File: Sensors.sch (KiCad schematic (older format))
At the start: 70 parts, among them CN3 CONN_HEADER_SMD_4POS_2MM, CN4 CONN_HEADER_SMD_4POS_2MM, U1 LPS25HB, U10 MPXV4006GP, U11 MPXV4006DP, U12 TLV2333IDR, U17 MPXV4006GP

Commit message: Annotation has been done
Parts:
- gave numbers to parts that had none: 43

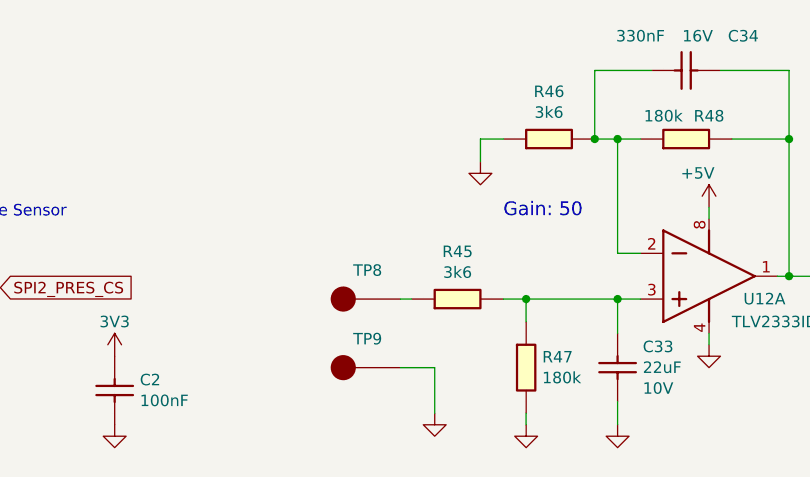
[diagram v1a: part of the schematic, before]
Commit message: added connectors for oxygen sensor and speakers molex 2.54mm pitch vertical
connectors have been added for oxygen sensor and speakers. thery are molex vertical connector 2.54mm pitch vertical. please let me know if any other part is desirable to be used instead.
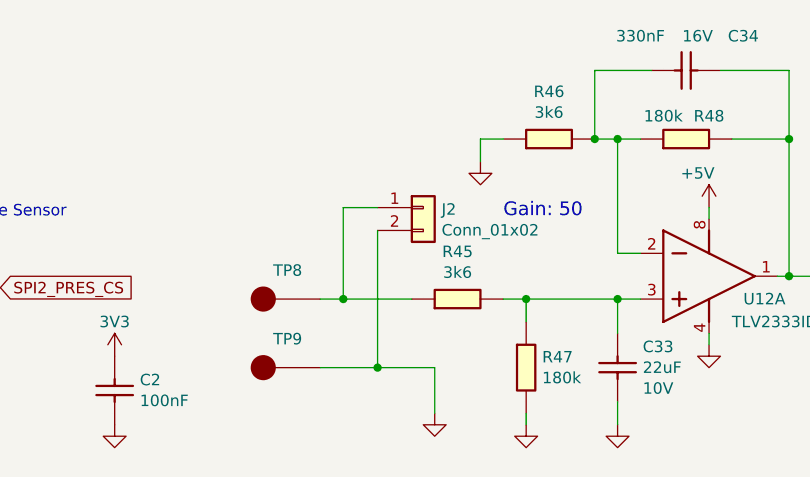
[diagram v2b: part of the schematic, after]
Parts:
- added J2: Conn_01x02, Connector_PinSocket_2.54mm:PinSocket_1x02_P2.54mm_Vertical, symbol Connector_Generic:Conn_01x02
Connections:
- net GND: now also J2.2 (Pin_2)
- net at R45.1, TP8.1: now also J2.1 (Pin_1)
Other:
- moved on the sheet: TP8, TP9
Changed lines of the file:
@@
 	2700 2100 2300 2100
 Wire Wire Line
-	4600 7250 4450 7250
-Wire Wire Line
 	4600 7450 4600 7250
-Wire Wire Line
-	4500 6950 4450 6950
 Wire Wire Line
 	5400 6950 5500 6950
@@
 L OpenVent:Test_Point_PTH TP8
 U 1 1 5FCEC103
-P 4450 6950
-F 0 "TP8" H 4307 7075 50  0000 C CNN
-F 1 "Test_Point_PTH" H 4450 6950 50  0001 C CNN
-F 2 "TestPoint:TestPoint_Pad_2.0x2.0mm" H 4450 6950 50  0001 C CNN
-F 3 "" H 4450 6950 50  0001 C CNN
-	1    4450 6950
+P 4100 6950
+F 0 "TP8" H 3957 7075 50  0000 C CNN
+F 1 "Test_Point_PTH" H 4100 6950 50  0001 C CNN
+F 2 "TestPoint:TestPoint_Pad_2.0x2.0mm" H 4100 6950 50  0001 C CNN
+F 3 "" H 4100 6950 50  0001 C CNN
+	1    4100 6950
 	1    0    0    -1
 $EndComp
@@
 L OpenVent:Test_Point_PTH TP9
 U 1 1 5FCECBB9
-P 4450 7250
-F 0 "TP9" H 4307 7375 50  0000 C CNN
-F 1 "Test_Point_PTH" H 4450 7250 50  0001 C CNN
-F 2 "TestPoint:TestPoint_Pad_2.0x2.0mm" H 4450 7250 50  0001 C CNN
-F 3 "" H 4450 7250 50  0001 C CNN
-	1    4450 7250
+P 4100 7250
+F 0 "TP9" H 3957 7375 50  0000 C CNN
+F 1 "Test_Point_PTH" H 4100 7250 50  0001 C CNN
+F 2 "TestPoint:TestPoint_Pad_2.0x2.0mm" H 4100 7250 50  0001 C CNN
+F 3 "" H 4100 7250 50  0001 C CNN
+	1    4100 7250
 	1    0    0    -1
 $EndComp
@@
 Text Notes 6450 4050 0    75   ~ 15
 FPGA ADC analog circuitry
+Wire Wire Line
+	4100 7250 4350 7250
+Wire Wire Line
+	4350 6650 4350 7250
+Connection ~ 4350 7250
+Wire Wire Line
+	4350 7250 4600 7250
+Wire Wire Line
+	4350 6550 4200 6550
+Wire Wire Line
+	4200 6550 4200 6950
+Wire Wire Line
+	4100 6950 4200 6950
+Connection ~ 4200 6950
+Wire Wire Line
+	4200 6950 4500 6950
+$Comp
+L Connector_Generic:Conn_01x02 J2
+U 1 1 609D2D12
+P 4550 6550
+AR Path="/5F8F3873/609D2D12" Ref="J2"  Part="1"
+AR Path="/60D4F569/609D2D12" Ref="J?"  Part="1"
+F 0 "J2" H 4630 6542 50  0000 L CNN
+F 1 "Conn_01x02" H 4630 6451 50  0000 L CNN
+F 2 "Connector_PinSocket_2.54mm:PinSocket_1x02_P2.54mm_Vertical" H 4550 6550 50  0001 C CNN
+F 3 "http://www.farnell.com/datasheets/2695416.pdf" H 4550 6550 50  0001 C CNN
+	1    4550 6550
+	1    0    0    -1
+$EndComp
 $EndSCHEMATC

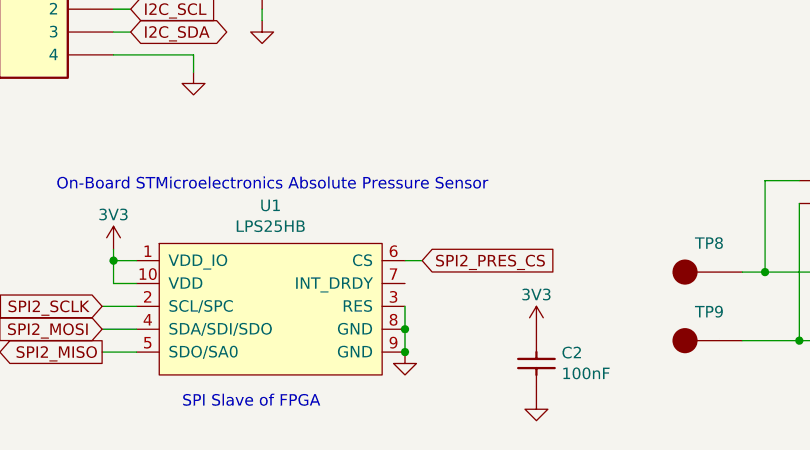
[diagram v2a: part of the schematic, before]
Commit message: Beginning the process of design review, fixed a couple howlers.
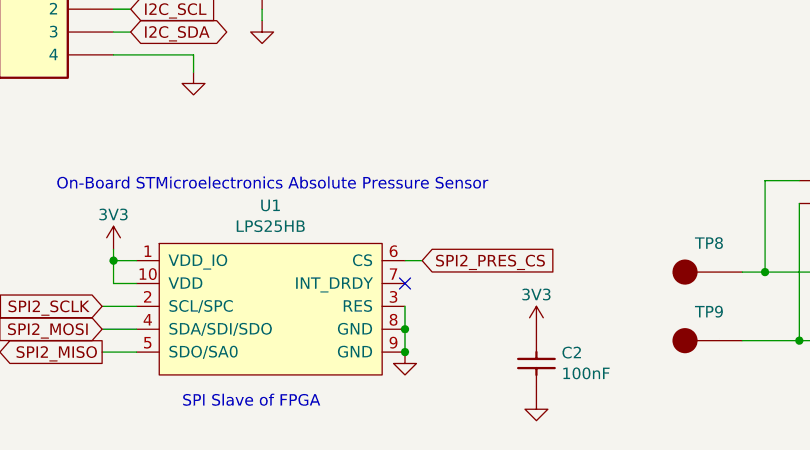
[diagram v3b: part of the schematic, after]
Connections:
- no-connect marks 1 -> 2
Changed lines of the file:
@@
 	1    0    0    -1
 $EndComp
+NoConn ~ 2625 7000
 $EndSCHEMATC

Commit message: add footprint
new footprint was added to parts without footprint
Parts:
- FB4: value Chip_Ferrite,_600R,_0603,_750mA -> BLM18AG601SN1D Chip_Ferrite,_600R,_0603,_750mA; footprint (none) -> Capacitor_SMD:C_0603_1608Metric
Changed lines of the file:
@@
 AR Path="/5F8F3873/61F2C4AF" Ref="FB4"  Part="1"
 F 0 "FB4" H 6900 1800 50  0000 C CNN
-F 1 "Chip_Ferrite,_600R,_0603,_750mA" H 6900 2008 50  0001 C CNN
-F 2 "" H 6600 1700 50  0001 C CNN
-F 3 "" H 6600 1700 50  0001 C CNN
+F 1 "BLM18AG601SN1D Chip_Ferrite,_600R,_0603,_750mA" H 6900 2008 50  0001 C CNN
+F 2 "Capacitor_SMD:C_0603_1608Metric" H 6600 1700 50  0001 C CNN
+F 3 "http://www.farnell.com/datasheets/1756147.pdf" H 6600 1700 50  0001 C CNN
 F 4 "600R" H 6750 1650 50  0000 C CNN "Val"
 F 5 "750mA" H 7050 1650 50  0000 C CNN "Current"

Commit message: Update Sensors.sch
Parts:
- removed R38: 100K_0603_Chip_Resistor,_1%,_0.1W, symbol OpenVent:100K_0603_Chip_Resistor,_1%,_0.1W
- added R38: R_0603_47K_0.1%_0.1W_Film, Resistor_SMD:R_0603_1608Metric_Pad0.98x0.95mm_HandSolder, symbol OpenVent:R_0603_47K_0.1%_0.1W_Film
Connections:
- net AD_VREF: now also R38.2
- net at U7.18 (1Y0): now also R38.1
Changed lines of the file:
@@
 	5800 7100 5800 7150
-$Comp
-L OpenVent:100K_0603_Chip_Resistor,_1%,_0.1W R?
-U 1 1 61F2C4A7
-P 8800 1500
-AR Path="/601B7AF8/61F2C4A7" Ref="R?"  Part="1"
-AR Path="/5F8F3873/61F2C4A7" Ref="R38"  Part="1"
-F 0 "R38" H 8900 1193 50  0000 C CNN
-F 1 "100K_0603_Chip_Resistor,_1%,_0.1W" H 8800 1500 50  0001 C CNN
-F 2 "" H 8800 1500 50  0001 C CNN
-F 3 "" H 8800 1500 50  0001 C CNN
-F 4 "100k" H 8900 1284 50  0000 C CNN "Val"
-F 5 "1%" H 8800 1500 50  0001 C CNN "Tolerance"
-F 6 "0.1W" H 8800 1500 50  0001 C CNN "Watt"
-	1    8800 1500
-	-1   0    0    1
-$EndComp
 $Comp
 L OpenVent:GND #PWR?
@@
 $EndComp
 NoConn ~ 2625 7000
+$Comp
+L OpenVent:R_0603_47K_0.1%_0.1W_Film R38
+U 1 1 60EB5CDA
+P 8600 1300
+F 0 "R38" H 8600 1300 50  0000 C CNN
+F 1 "R_0603_47K_0.1%_0.1W_Film" H 8600 1300 50  0001 C CNN
+F 2 "Resistor_SMD:R_0603_1608Metric_Pad0.98x0.95mm_HandSolder" H 8600 1300 50  0001 C CNN
+F 3 "https://www.digikey.com/en/products/filter/chip-resistor-surface-mount/52" H 8600 1300 50  0001 C CNN
+F 4 "47k" H 8800 1300 50  0000 C CNN "Val"
+F 5 "0.1%" H 8700 1100 50  0000 C CNN "Tolerance"
+F 6 "0.1W" H 8600 1300 50  0001 C CNN "Watt"
+F 7 "KOA Speer Electronics, Inc." H 8600 1300 50  0001 C CNN "Mfr"
+F 8 "RN73H1JTTD4702B25" H 8600 1300 50  0001 C CNN "Mfr_PN"
+F 9 "RES 47K OHM 0.1% 1/10W 0603" H 8600 1300 50  0001 C CNN "Desc"
+F 10 "47 kOhms ±0.1% 0.1W, 1/10W Chip Resistor 0603 (1608 Metric) Automotive AEC-Q200, Moisture Resistant Metal Film" H 8600 1300 50  0001 C CNN "Detailed"
+	1    8600 1300
+	1    0    0    -1
+$EndComp
 $EndSCHEMATC

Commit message: Update Sensors.sch
U12B impedance matched
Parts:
- removed R27: 18k_0603_Chip_Resistor,_1%,_0.1W, Resistor_SMD:R_0603_1608Metric, symbol OpenVent:18k_0603_Chip_Resistor,_1%,_0.1W
- removed R32: 100K_0603_Chip_Resistor,_1%,_0.1W, symbol OpenVent:100K_0603_Chip_Resistor,_1%,_0.1W
- removed R37: 215k_0603_Chip_Resistor,_1%,_0.1W, Resistor_SMD:R_0603_1608Metric, symbol OpenVent:215k_0603_Chip_Resistor,_1%,_0.1W
- added R27, R37: 133k_0603_Chip_Resistor,_1%,_0.1W, Resistor_SMD:R_0603_1608Metric, symbol OpenVent:133k_0603_Chip_Resistor,_1%,_0.1W
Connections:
- wire segments 263 -> 262
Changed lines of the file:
@@
-	1    0    0    -1
-$EndComp
-$Comp
-L OpenVent:215k_0603_Chip_Resistor,_1%,_0.1W R37
-U 1 1 5F8DD09B
-P 3200 1500
-F 0 "R37" H 3200 1450 50  0000 L BNN
-F 1 "215k_0603_Chip_Resistor,_1%,_0.1W" H 3200 1250 50  0001 C CNN
-F 2 "Resistor_SMD:R_0603_1608Metric" H 3200 1160 60  0001 C CNN
-F 3 "" H 3200 1160 60  0001 C CNN
-F 4 "1%" V 1200 -2800 50  0001 C CNN "Tolerance"
-F 5 "215k" H 3300 1300 50  0000 C CNN "Val"
-F 6 "0.1W" H 3200 1500 50  0001 C CNN "Watt"
-	1    3200 1500
 	1    0    0    -1
 $EndComp
@@
 $EndComp
 $Comp
-L OpenVent:18k_0603_Chip_Resistor,_1%,_0.1W R27
-U 1 1 5FF283BF
-P 3100 950
-F 0 "R27" H 3200 1057 50  0000 C CNN
-F 1 "18k_0603_Chip_Resistor,_1%,_0.1W" H 3030 550 50  0001 C CNN
-F 2 "Resistor_SMD:R_0603_1608Metric" H 2980 1190 50  0001 C CNN
-F 3 "" H 3100 950 50  0001 C CNN
-F 4 "18k" H 3200 966 50  0000 C CNN "Val"
-F 5 "1%" H 3160 660 50  0001 C CNN "Tolerance"
-F 6 "0.1W" H 3800 940 50  0001 C CNN "Watt"
-	1    3100 950
-	1    0    0    -1
-$EndComp
-$Comp
 L OpenVent:GND #GND_044
 U 1 1 5FF4487C
@@
 Wire Wire Line
 	2550 1700 2550 1500
-Wire Wire Line
-	2950 1050 3000 1050
 Connection ~ 3900 1050
 Wire Wire Line
@@
 Wire Wire Line
 	3900 1050 3900 1400
-Wire Wire Line
-	3400 1050 3450 1050
-$Comp
-L OpenVent:100K_0603_Chip_Resistor,_1%,_0.1W R32
-U 1 1 5FF27B3E
-P 3550 950
-F 0 "R32" H 3650 1057 50  0000 C CNN
-F 1 "100K_0603_Chip_Resistor,_1%,_0.1W" H 3550 950 50  0001 C CNN
-F 2 "" H 3550 950 50  0001 C CNN
-F 3 "" H 3550 950 50  0001 C CNN
-F 4 "100k" H 3650 966 50  0000 C CNN "Val"
-F 5 "1%" H 3550 950 50  0001 C CNN "Tolerance"
-F 6 "0.1W" H 3550 950 50  0001 C CNN "Watt"
-	1    3550 950
-	1    0    0    -1
-$EndComp
-Wire Wire Line
-	3850 1050 3900 1050
 Connection ~ 5000 6950
 Wire Wire Line
@@
 	1    0    0    -1
 $EndComp
+$Comp
+L OpenVent:133k_0603_Chip_Resistor,_1%,_0.1W R37
+U 1 1 60FC5F82
+P 3300 1600
+F 0 "R37" H 3300 1807 50  0000 C CNN
+F 1 "133k_0603_Chip_Resistor,_1%,_0.1W" H 3130 1300 50  0001 C CNN
+F 2 "Resistor_SMD:R_0603_1608Metric" H 3080 1940 50  0001 C CNN
+F 3 "" H 3200 1700 50  0001 C CNN
+F 4 "133k" H 3300 1716 50  0000 C CNN "Val"
+F 5 "1%" H 3260 1410 50  0001 C CNN "Tolerance"
+F 6 "0.1W" H 3900 1690 50  0001 C CNN "Watt"
+	1    3300 1600
+	1    0    0    -1
+$EndComp
+$Comp
+L OpenVent:133k_0603_Chip_Resistor,_1%,_0.1W R27
+U 1 1 6100D46A
+P 3500 1050
+F 0 "R27" H 3500 1257 50  0000 C CNN
+F 1 "133k_0603_Chip_Resistor,_1%,_0.1W" H 3330 750 50  0001 C CNN
+F 2 "Resistor_SMD:R_0603_1608Metric" H 3280 1390 50  0001 C CNN
+F 3 "" H 3400 1150 50  0001 C CNN
+F 4 "133k" H 3500 1166 50  0000 C CNN "Val"
+F 5 "1%" H 3460 860 50  0001 C CNN "Tolerance"
+F 6 "0.1W" H 4100 1140 50  0001 C CNN "Watt"
+	1    3500 1050
+	1    0    0    -1
+$EndComp
+Wire Wire Line
+	3700 1050 3900 1050
+Wire Wire Line
+	2950 1050 3300 1050
 $EndSCHEMATC

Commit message: footprint added to 99%
99% of parts have footprint now.
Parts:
- CN3, CN4: footprint (none) -> OpenVent_Footprint_Test:SMT_4pos_2mm
- TP1, TP10, TP2, TP3, TP4, TP5, TP6, TP7: footprint (none) -> TestPoint:TestPoint_THTPad_2.0x2.0mm_Drill1.0mm
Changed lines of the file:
@@
 F 0 "CN3" H 1593 6475 50  0000 C CNN
 F 1 "CONN_HEADER_SMD_4POS_2MM" H 1650 5800 50  0001 C CNN
-F 2 "" H 1550 6400 50  0001 C CNN
+F 2 "OpenVent_Footprint_Test:SMT_4pos_2mm" H 1550 6400 50  0001 C CNN
 F 3 "" H 1550 6400 50  0001 C CNN
 	1    1350 6000
@@
 F 0 "CN4" H 1493 1775 50  0000 C CNN
 F 1 "CONN_HEADER_SMD_4POS_2MM" H 1550 1100 50  0001 C CNN
-F 2 "" H 1450 1700 50  0001 C CNN
+F 2 "OpenVent_Footprint_Test:SMT_4pos_2mm" H 1450 1700 50  0001 C CNN
 F 3 "" H 1450 1700 50  0001 C CNN
 	1    1250 1300
@@
 F 0 "TP3" H 9620 2700 50  0000 R CNN
 F 1 "Test_Point_PTH" H 9950 2700 50  0001 C CNN
-F 2 "" H 9950 2700 50  0001 C CNN
-F 3 "" H 9950 2700 50  0001 C CNN
+F 2 "TestPoint:TestPoint_THTPad_2.0x2.0mm_Drill1.0mm" H 9950 2700 50  0001 C CNN
+F 3 "https://www.farnell.com/datasheets/62443.pdf" H 9950 2700 50  0001 C CNN
 	1    9950 2700
 	-1   0    0    1
@@
 F 0 "TP4" H 9620 3350 50  0000 R CNN
 F 1 "Test_Point_PTH" H 9950 3350 50  0001 C CNN
-F 2 "" H 9950 3350 50  0001 C CNN
-F 3 "" H 9950 3350 50  0001 C CNN
+F 2 "TestPoint:TestPoint_THTPad_2.0x2.0mm_Drill1.0mm" H 9950 3350 50  0001 C CNN
+F 3 "https://www.farnell.com/datasheets/62443.pdf" H 9950 3350 50  0001 C CNN
 	1    9950 3350
 	-1   0    0    1
@@
 F 0 "TP5" H 9620 4000 50  0000 R CNN
 F 1 "Test_Point_PTH" H 9950 4000 50  0001 C CNN
-F 2 "" H 9950 4000 50  0001 C CNN
-F 3 "" H 9950 4000 50  0001 C CNN
+F 2 "TestPoint:TestPoint_THTPad_2.0x2.0mm_Drill1.0mm" H 9950 4000 50  0001 C CNN
+F 3 "https://www.farnell.com/datasheets/62443.pdf" H 9950 4000 50  0001 C CNN
 	1    9950 4000
 	-1   0    0    1
@@
 F 0 "TP6" H 9620 4650 50  0000 R CNN
 F 1 "Test_Point_PTH" H 9950 4650 50  0001 C CNN
-F 2 "" H 9950 4650 50  0001 C CNN
-F 3 "" H 9950 4650 50  0001 C CNN
+F 2 "TestPoint:TestPoint_THTPad_2.0x2.0mm_Drill1.0mm" H 9950 4650 50  0001 C CNN
+F 3 "https://www.farnell.com/datasheets/62443.pdf" H 9950 4650 50  0001 C CNN
 	1    9950 4650
 	-1   0    0    1
@@
 F 0 "TP7" H 9620 5300 50  0000 R CNN
 F 1 "Test_Point_PTH" H 9950 5300 50  0001 C CNN
-F 2 "" H 9950 5300 50  0001 C CNN
-F 3 "" H 9950 5300 50  0001 C CNN
+F 2 "TestPoint:TestPoint_THTPad_2.0x2.0mm_Drill1.0mm" H 9950 5300 50  0001 C CNN
+F 3 "https://www.farnell.com/datasheets/62443.pdf" H 9950 5300 50  0001 C CNN
 	1    9950 5300
 	-1   0    0    1
@@
 F 0 "TP10" H 9620 5950 50  0000 R CNN
 F 1 "Test_Point_PTH" H 9950 5950 50  0001 C CNN
-F 2 "" H 9950 5950 50  0001 C CNN
-F 3 "" H 9950 5950 50  0001 C CNN
+F 2 "TestPoint:TestPoint_THTPad_2.0x2.0mm_Drill1.0mm" H 9950 5950 50  0001 C CNN
+F 3 "https://www.farnell.com/datasheets/62443.pdf" H 9950 5950 50  0001 C CNN
 	1    9950 5950
 	-1   0    0    1
@@
 F 0 "TP1" V 9057 1430 50  0000 L CNN
 F 1 "Test_Point_PTH" H 9200 1350 50  0001 C CNN
-F 2 "" H 9200 1350 50  0001 C CNN
-F 3 "" H 9200 1350 50  0001 C CNN
+F 2 "TestPoint:TestPoint_THTPad_2.0x2.0mm_Drill1.0mm" H 9200 1350 50  0001 C CNN
+F 3 "https://www.farnell.com/datasheets/62443.pdf" H 9200 1350 50  0001 C CNN
 	1    9200 1350
 	0    1    1    0
@@
 F 0 "TP2" H 9620 2150 50  0000 R CNN
 F 1 "Test_Point_PTH" H 9950 2150 50  0001 C CNN
-F 2 "" H 9950 2150 50  0001 C CNN
-F 3 "" H 9950 2150 50  0001 C CNN
+F 2 "TestPoint:TestPoint_THTPad_2.0x2.0mm_Drill1.0mm" H 9950 2150 50  0001 C CNN
+F 3 "Mellisa added" H 9950 2150 50  0001 C CNN
 	1    9950 2150
 	-1   0    0    1

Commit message: Updated the project to include a M2GL010-1TQG144 IGLOO2 FPGA instead of the GOWIN. Since the IGLOO has some 2.5V BANKs as well as 3.3V Banks, some circuitry will need to be modified elsewhere in the circuit, but most of the interfaces are easily changeable, be it different power supplies or the additions of transistors or potential dividers. I will edit the rest of the design later, and write up a list of things I changed for the other peeps in the design team to review
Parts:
- added C? (x4): 100nF_0603_Ceramic_Capacitor,_10%,_X7R,_25V, symbol OpenVent:100nF_0603_Ceramic_Capacitor,_10%,_X7R,_25V
- added C?: 10uF_0805_Ceramic_Capacitor_10%_X7R_10V, Capacitor_SMD:C_0805_2012Metric, symbol OpenVent:10uF_0805_Ceramic_Capacitor_10%_X7R_10V
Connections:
- wire segments 262 -> 281
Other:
- note added: "Bypass Caps for Power Block"
- note added: "These might break the FPGA\n"
- moved on the sheet: C33, C34, C35, J2, R45, R46, R47, R48, TP8, TP9, U12A
